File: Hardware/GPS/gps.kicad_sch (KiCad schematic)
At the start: 0 parts

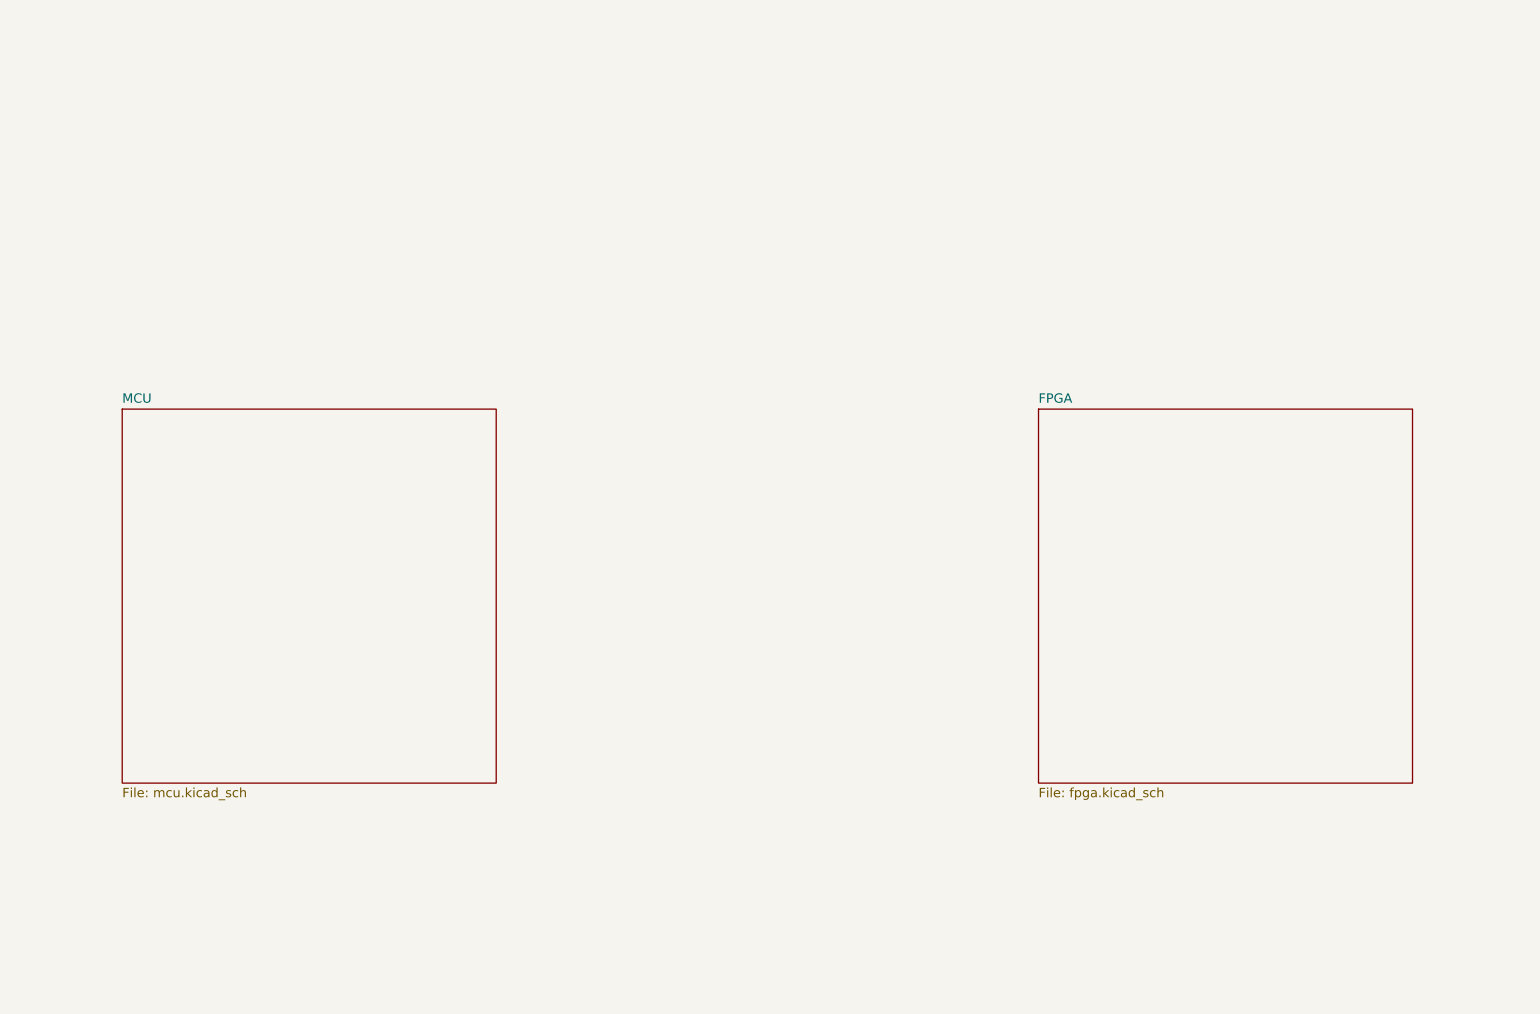
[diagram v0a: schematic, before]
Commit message: Major updates to Simulator and hardware
- Simulator has functional acquisition for L1CA, E1C, B1C, L1C.
- Simulator can track, decode, and solve for position on L1CA and E1C.
- Development on custom hardware
- Created Pi Pico 2 development environment for prototyping.
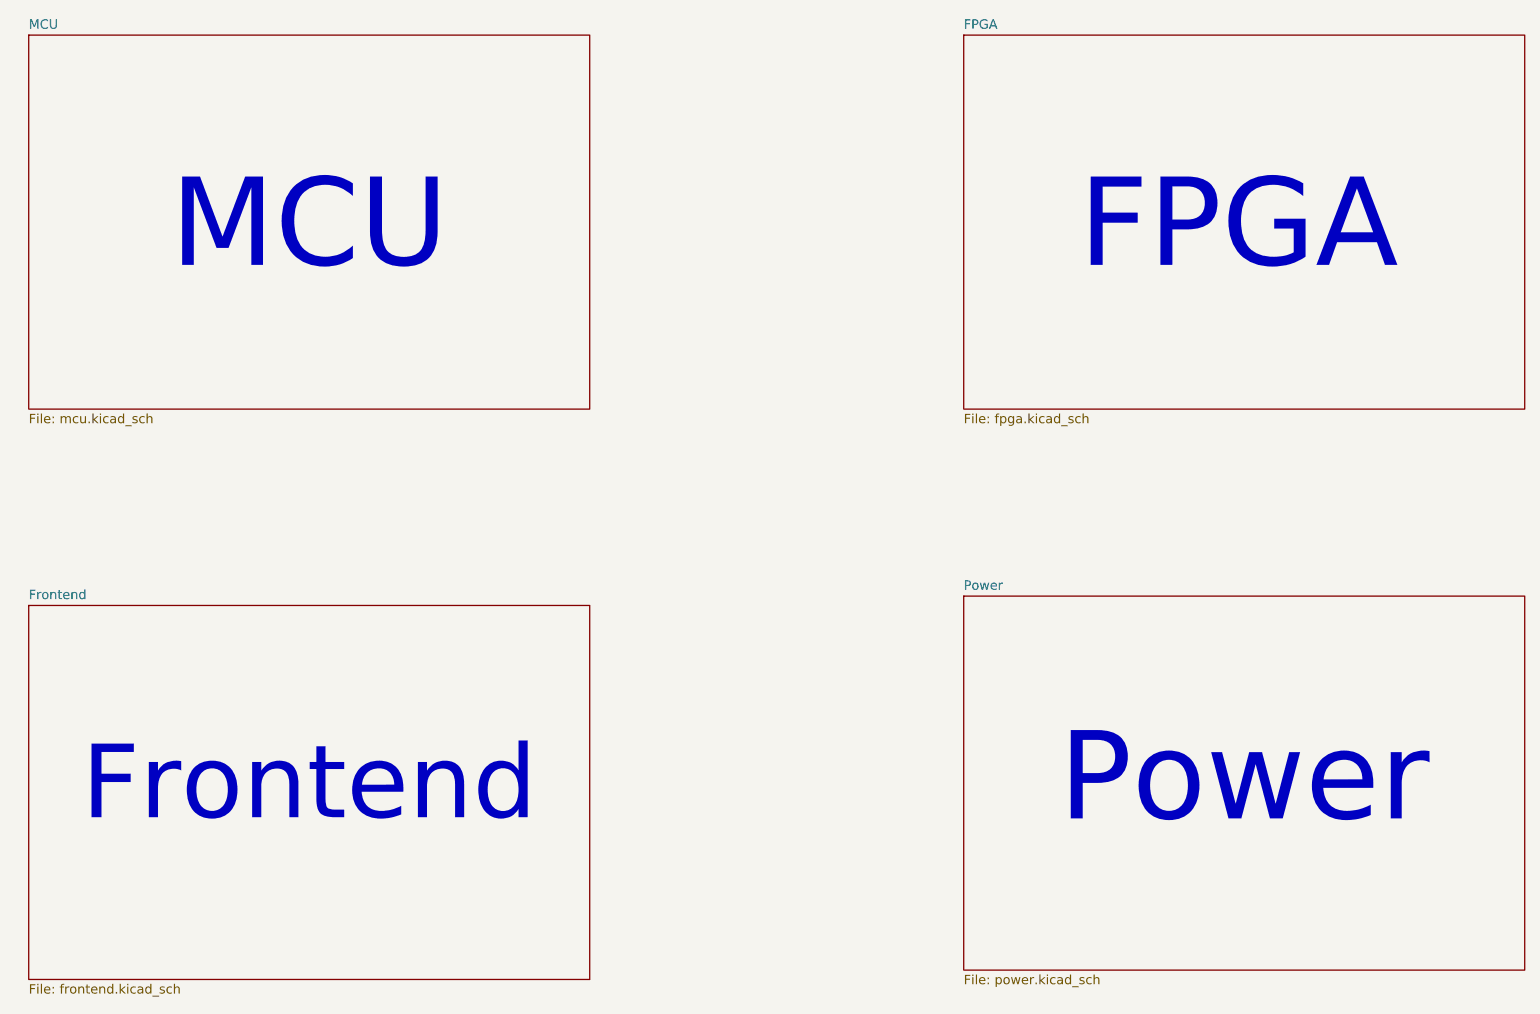
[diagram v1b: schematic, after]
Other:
- added sheet Frontend (frontend.kicad_sch)
- added sheet Power (power.kicad_sch)
- note added: "FPGA"
- note added: "Frontend"
- note added: "MCU"
- note added: "Power"
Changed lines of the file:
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@@
 	(generator_version "10.0")
 	(paper "A4")
-	(sheet
-		(at 63.5 76.2)
-		(size 50.8 50.8)
+	(text "Frontend"
+		(exclude_from_sim no)
+		(at 88.9 127.254 0)
+		(effects
+			(font
+				(size 10 10)
+			)
+		)
+	)
+	(text "MCU"
+		(exclude_from_sim no)
+		(at 88.9 51.308 0)
+		(effects
+			(font
+				(size 12 12)
+			)
+		)
+	)
+	(text "Power"
+		(exclude_from_sim no)
+		(at 215.9 126.492 0)
+		(effects
+			(font
+				(size 12 12)
+			)
+		)
+	)
+	(text "FPGA"
+		(exclude_from_sim no)
+		(at 215.138 51.308 0)
+		(effects
+			(font
+				(size 12 12)
+			)
+		)
+	)
+	(sheet
+		(at 50.8 25.4)
+		(size 76.2 50.8)
 		(exclude_from_sim no)
 		(in_bom yes)
@@
 		)
 		(property "Sheetname" "MCU"
-			(at 63.5 75.4884 0)
+			(at 50.8 24.6884 0)
 			(show_name no)
 			(do_not_autoplace no)
@@
 		)
 		(property "Sheetfile" "mcu.kicad_sch"
-			(at 63.5 127.5846 0)
+			(at 50.8 76.7846 0)
 			(show_name no)
 			(do_not_autoplace no)
@@
 		)
 		(property "Field2" ""
-			(at 63.5 76.2 0)
+			(at 50.8 25.4 0)
 			(hide yes)
 			(show_name no)
@@
 	)
 	(sheet
-		(at 187.96 76.2)
-		(size 50.8 50.8)
+		(at 50.8 102.87)
+		(size 76.2 50.8)
+		(exclude_from_sim no)
+		(in_bom yes)
+		(on_board yes)
+		(dnp no)
+		(fields_autoplaced yes)
+		(stroke
+			(width 0.1524)
+			(type solid)
+		)
+		(fill
+			(color 0 0 0 0)
+		)
+		(property "Sheetname" "Frontend"
+			(at 50.8 102.1584 0)
+			(show_name no)
+			(do_not_autoplace no)
+			(effects
+				(font
+					(size 1.27 1.27)
+				)
+				(justify left bottom)
+			)
+		)
+		(property "Sheetfile" "frontend.kicad_sch"
+			(at 50.8 154.2546 0)
+			(show_name no)
+			(do_not_autoplace no)
+			(effects
+				(font
+					(size 1.27 1.27)
+				)
+				(justify left top)
+			)
+		)
+		(property "Field2" ""
+			(at 50.8 102.87 0)
+			(hide yes)
+			(show_name no)
+			(do_not_autoplace no)
+			(effects
+				(font
+					(size 1.27 1.27)
+				)
+			)
+		)
+		(instances
+			(project "gps"
+				(path "/61c049dc-805b-4562-a164-b3263a6a0d84"
+					(page "4")
+				)
+			)
+		)
+	)
+	(sheet
+		(at 177.8 25.4)
+		(size 76.2 50.8)
 		(exclude_from_sim no)
 		(in_bom yes)
@@
 		)
 		(property "Sheetname" "FPGA"
-			(at 187.96 75.4884 0)
+			(at 177.8 24.6884 0)
 			(show_name no)
 			(do_not_autoplace no)
@@
 		)
 		(property "Sheetfile" "fpga.kicad_sch"
-			(at 187.96 127.5846 0)
+			(at 177.8 76.7846 0)
 			(show_name no)
 			(do_not_autoplace no)
@@
 		)
 		(property "Field2" ""
-			(at 187.96 76.2 0)
+			(at 177.8 25.4 0)
 			(hide yes)
 			(show_name no)
@@
 				)
 			)
+		)
+	)
+	(sheet
+		(at 177.8 101.6)
+		(size 76.2 50.8)
+		(exclude_from_sim no)
+		(in_bom yes)
+		(on_board yes)
+		(dnp no)
+		(fields_autoplaced yes)
+		(stroke
+			(width 0.1524)
+			(type solid)
+		)
+		(fill
+			(color 0 0 0 0)
+		)
+		(property "Sheetname" "Power"
+			(at 177.8 100.8884 0)
+			(show_name no)
+			(do_not_autoplace no)
+			(effects
+				(font
+					(size 1.27 1.27)
+				)
+				(justify left bottom)
+			)
+		)
+		(property "Sheetfile" "power.kicad_sch"
+			(at 177.8 152.9846 0)
+			(show_name no)
+			(do_not_autoplace no)
+			(effects
+				(font
+					(size 1.27 1.27)
+				)
+				(justify left top)
+			)
+		)
+		(instances
+			(project "gps"
+				(path "/61c049dc-805b-4562-a164-b3263a6a0d84"
+					(page "5")
+				)
+			)
